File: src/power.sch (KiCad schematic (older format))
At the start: 26 parts

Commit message: fix libraries on macos
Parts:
- removed U?: STC3115AIJT, CSP-10_STM, symbol gas_gauge:STC3115AIJT
- added U?: STC3115AIJT, CSP-10_STM, symbol 2021-10-23_16-14-28:STC3115AIJT
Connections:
- net GG_ALM: now also U?.A1 (ALM)
- net GG_BATD: now also U?.B2 (BATDCD)
- net GG_CG: now also U?.D3 (CG)
- net GG_RSTIO: now also U?.C3 (RSTIO)
- net GG_SCL: now also U?.C1 (SCL)
- net GG_SDA: now also U?.B1 (SDA)
- net GND: now also U?.D1 (GND)
- net VOUT: now also U?.A3 (VIN), U?.B3 (VCC)
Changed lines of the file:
@@
-$EndComp
-$Comp
-L gas_gauge:STC3115AIJT U?
-U 1 1 6177B179
-P 5900 1200
-AR Path="/6177B179" Ref="U?"  Part="1"
-AR Path="/61773D02/6177B179" Ref="U?"  Part="1"
-F 0 "U?" H 6800 1587 60  0000 C CNN
-F 1 "STC3115AIJT" H 6800 1481 60  0000 C CNN
-F 2 "CSP-10_STM" H 6800 1440 60  0001 C CNN
-F 3 "" H 5900 1200 60  0000 C CNN
-	1    5900 1200
-	1    0    0    -1
 $EndComp
 $Comp
@@
 	5450 1400 5500 1400
 Connection ~ 5500 1400
+$Comp
+L 2021-10-23_16-14-28:STC3115AIJT U?
+U 1 1 617BA6B9
+P 5900 1200
+F 0 "U?" H 6800 1587 60  0000 C CNN
+F 1 "STC3115AIJT" H 6800 1481 60  0000 C CNN
+F 2 "CSP-10_STM" H 6800 1440 60  0001 C CNN
+F 3 "" H 5900 1200 60  0000 C CNN
+	1    5900 1200
+	1    0    0    -1
+$EndComp
 $EndSCHEMATC

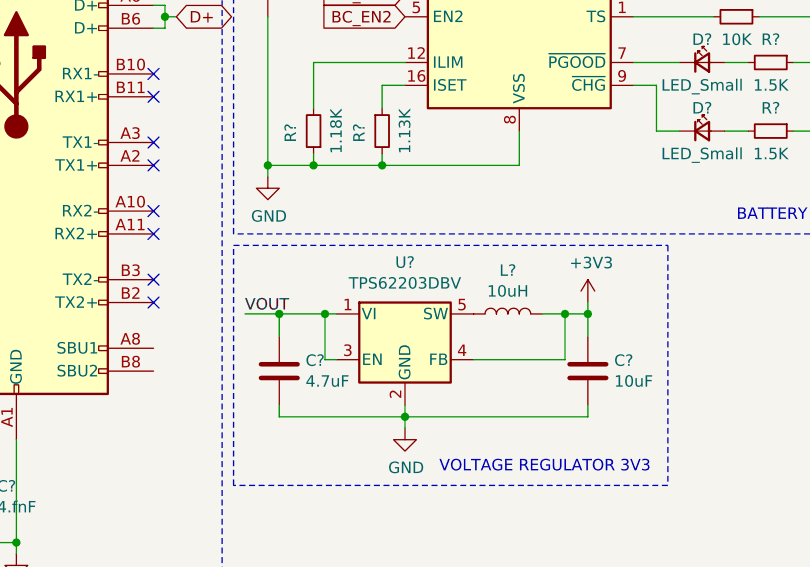
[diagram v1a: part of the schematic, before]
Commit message: switch MCU to STM32G0-series
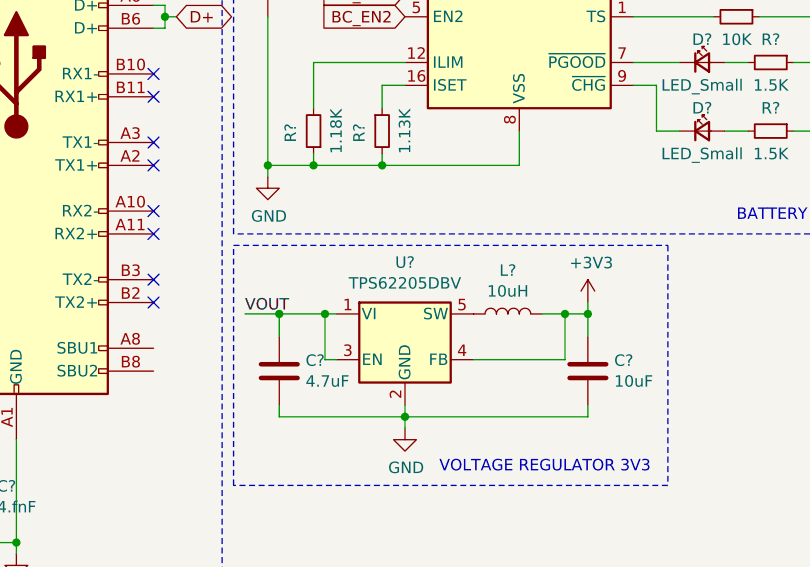
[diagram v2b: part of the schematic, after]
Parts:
- removed U?: TPS62203DBV, Package_TO_SOT_SMD:SOT-23-5, symbol Regulator_Switching:TPS62203DBV
- added U?: TPS62205DBV, Package_TO_SOT_SMD:SOT-23-5, symbol Regulator_Switching:TPS62205DBV
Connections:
- net +3V3: now also U?.4 (FB)
- net GND: now also U?.2 (GND)
- net VOUT: now also U?.1 (VI), U?.3 (EN)
- net at L?.1: now also U?.5 (SW)
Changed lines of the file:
@@
-$EndComp
-$Comp
-L Regulator_Switching:TPS62203DBV U?
-U 1 1 6177B173
-P 2800 3100
-AR Path="/6177B173" Ref="U?"  Part="1"
-AR Path="/61773D02/6177B173" Ref="U?"  Part="1"
-F 0 "U?" H 2800 3525 50  0000 C CNN
-F 1 "TPS62203DBV" H 2800 3434 50  0000 C CNN
-F 2 "Package_TO_SOT_SMD:SOT-23-5" H 2850 2950 50  0001 L CIN
-F 3 "http://www.ti.com/lit/ds/symlink/tps62201.pdf" H 2800 3200 50  0001 C CNN
-	1    2800 3100
-	1    0    0    -1
 $EndComp
 $Comp
@@
 	1    0    0    -1
 $EndComp
+$Comp
+L Regulator_Switching:TPS62205DBV U?
+U 1 1 617F3262
+P 2800 3100
+F 0 "U?" H 2800 3525 50  0000 C CNN
+F 1 "TPS62205DBV" H 2800 3434 50  0000 C CNN
+F 2 "Package_TO_SOT_SMD:SOT-23-5" H 2850 2950 50  0001 L CIN
+F 3 "http://www.ti.com/lit/ds/symlink/tps62201.pdf" H 2800 3200 50  0001 C CNN
+	1    2800 3100
+	1    0    0    -1
+$EndComp
